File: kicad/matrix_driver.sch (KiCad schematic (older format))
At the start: 54 parts, among them U10 DMN601, U11 NSI45015, U12 SN54LV574, U13 P-FET, U14 NSI45015, U15 DMN601, U16 NSI45015, U17 NSI45015, U18 DMN601, U19 P-FET, U20 NSI45015, U21 74HCT595, U22 NSI45015, U23 DMN601, U24 NSI45015, U25 P-FET, U26 NSI45015, U27 DMN601, U28 NSI45015, U29 SN54LV574, U30 NSI45015, U31 DMN601, U32 NSI45015, U33 P-FET, U34 NSI45015, U35 DMN601, U36 NSI45015, U37 NSI45015, U38 P-FET, U39 DMN601, U40 NSI45015, U41 NSI45015, U42 DMN601, U43 NSI45015, U44 SN54LV574, U45 74HCT595, U46 P-FET, U47 NSI45015, U48 DMN601, U49 NSI45015, U5 NSI45015, U50 NSI45015, U51 DMN601, U52 P-FET, U53 NSI45015, U6 P-FET, U7 DMN601, U8 NSI45015, U9 NSI45015

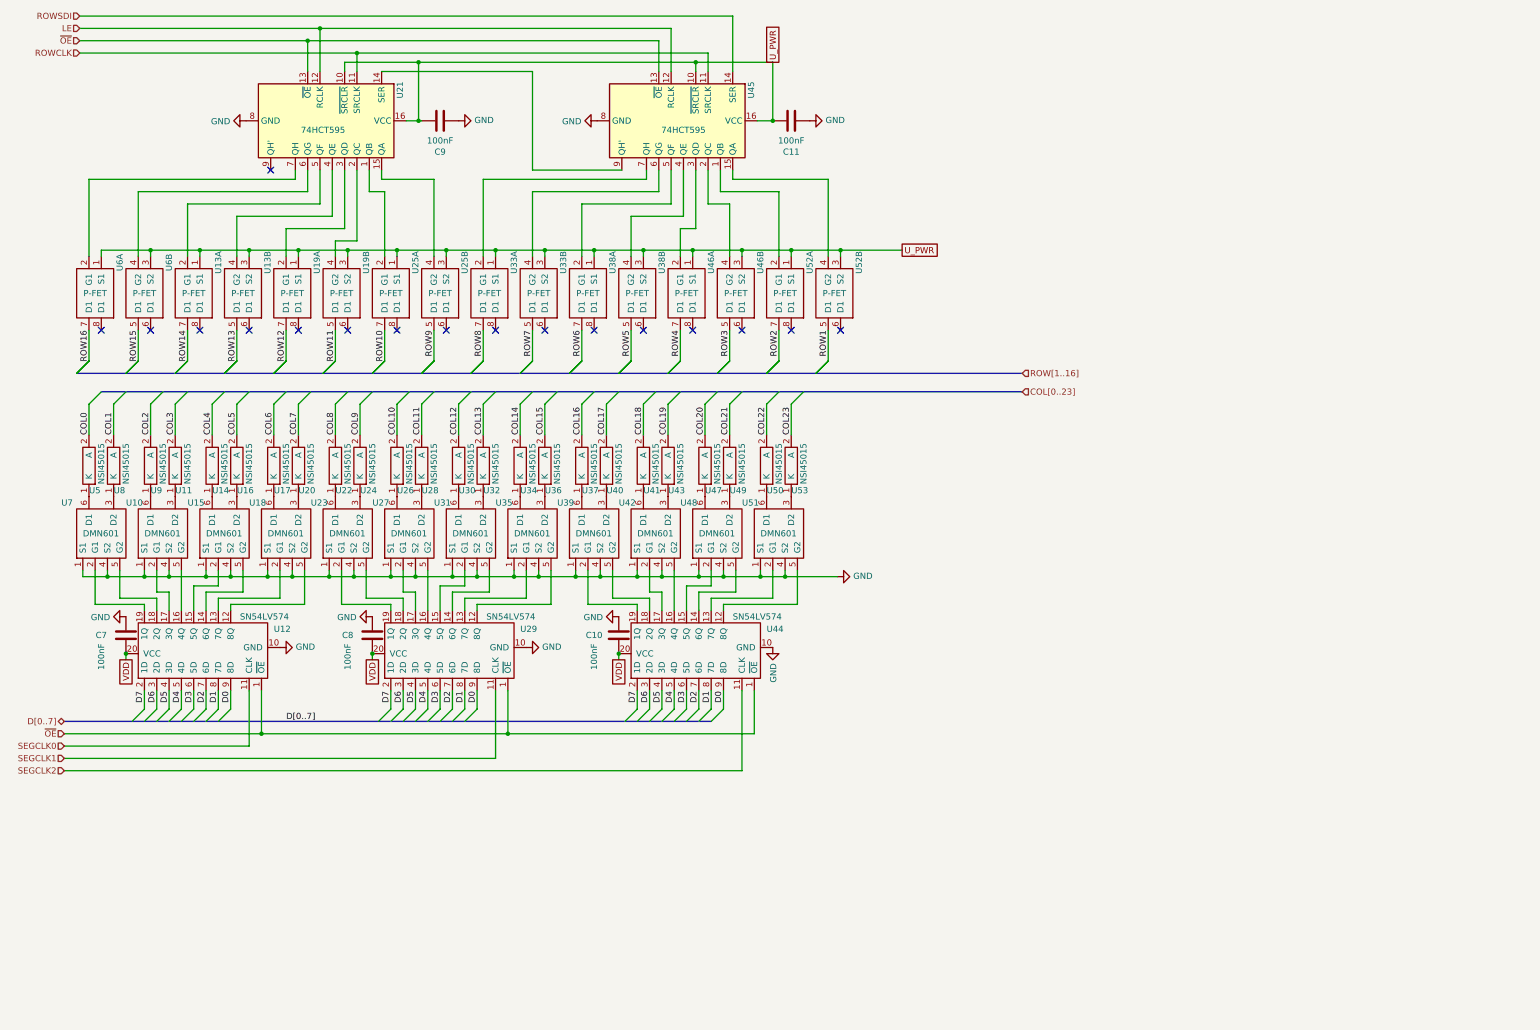
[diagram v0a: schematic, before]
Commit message: Adding level shifters
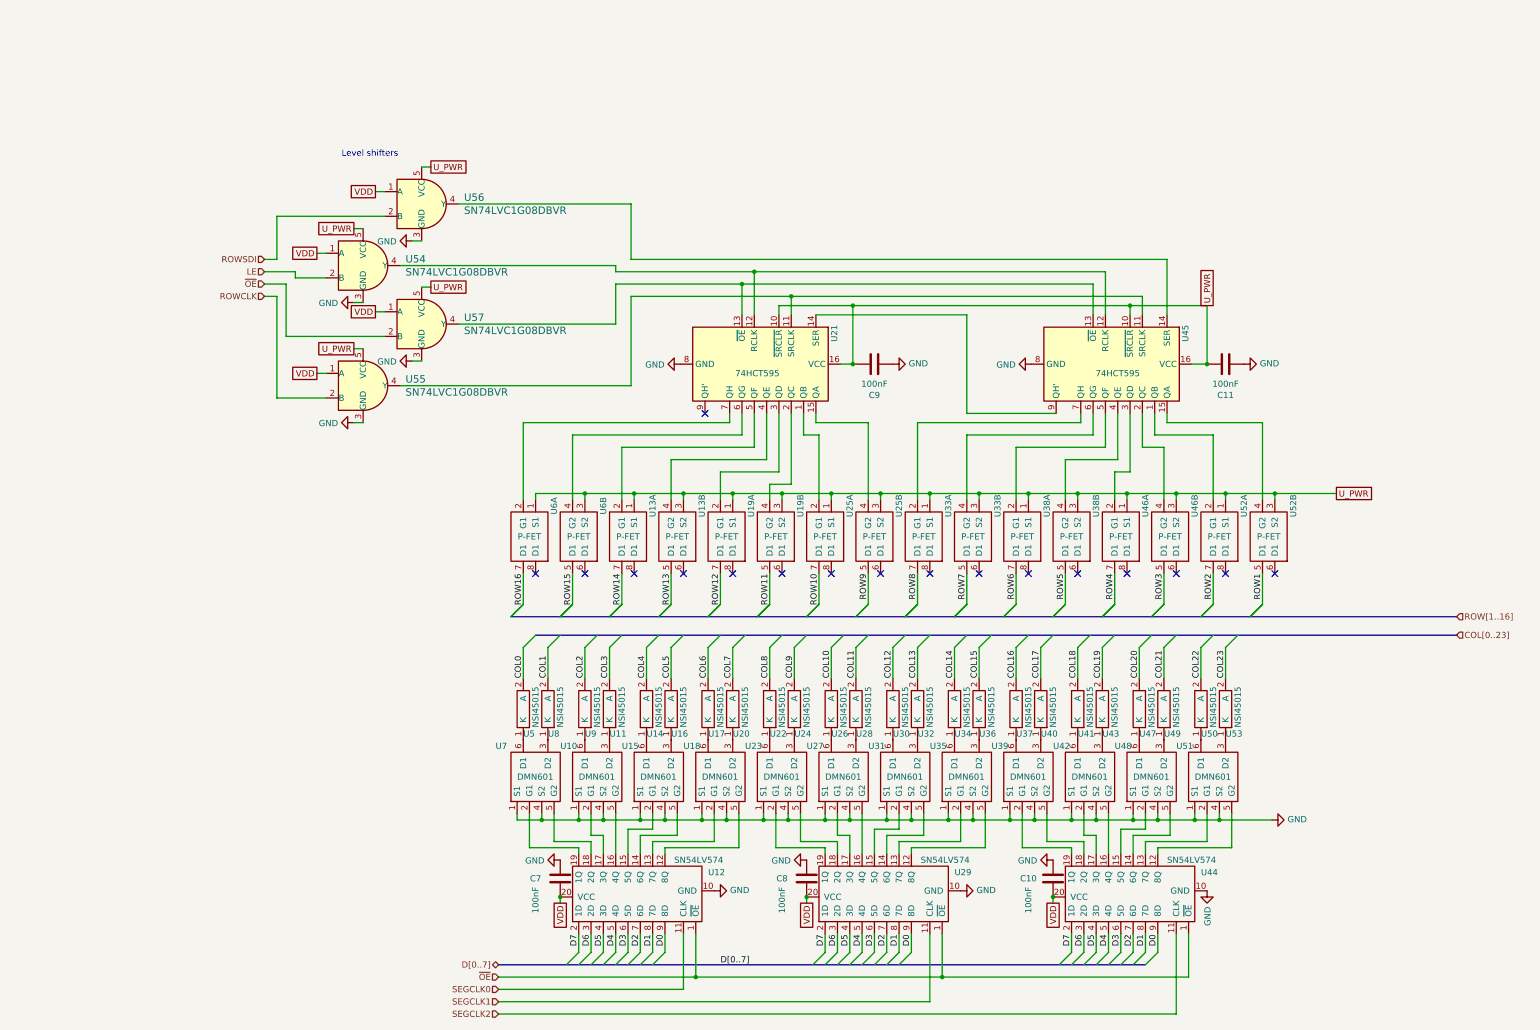
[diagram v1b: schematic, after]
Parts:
- added U54, U55, U56, U57: SN74LVC1G08DBVR, Package_TO_SOT_SMD:SOT-23-5, symbol dk_Logic-Gates-and-Inverters:SN74LVC1G08DBVR
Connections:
- net GND: now also U54.3 (GND), U55.3 (GND), U56.3 (GND), U57.3 (GND)
- net LE: now also U54.2 (B); no longer U21.12 (RCLK), U45.12 (RCLK)
- net ROWCLK: now also U55.2 (B); no longer U21.11 (SRCLK), U45.11 (SRCLK)
- net ROWSDI: now also U56.2 (B); no longer U45.14 (SER)
- net U_PWR: now also U54.5 (VCC), U55.5 (VCC), U56.5 (VCC), U57.5 (VCC)
- net VDD: now also U54.1 (A), U55.1 (A), U56.1 (A), U57.1 (A)
- net ~OE: now also U57.2 (B); no longer U21.13 (~OE), U45.13 (~OE)
- new net: U45.14 (SER), U56.4 (Y)
- new net: U21.13 (~OE), U45.13 (~OE), U57.4 (Y)
- new net: U21.12 (RCLK), U45.12 (RCLK), U54.4 (Y)
- new net: U21.11 (SRCLK), U45.11 (SRCLK), U55.4 (Y)
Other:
- note added: "Level shifters"
- moved on the sheet: C10, C11, C7, C8, C9, U10, U11, U12, U13A, U13B, U14, U15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

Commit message: Fix register footprints and add batt indicator
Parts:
- U12, U29, U44: footprint Package_SO:SO-20_5.3x12.6mm_P1.27mm -> Package_SO:SSOP-20_5.3x7.2mm_P0.65mm
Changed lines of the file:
@@
 F 0 "U44" V 9850 7375 50  0000 R CNN
 F 1 "SN54LV574" V 9950 7650 50  0000 R CNN
-F 2 "Package_SO:SO-20_5.3x12.6mm_P1.27mm" H 9700 7375 50  0001 C CNN
+F 2 "Package_SO:SSOP-20_5.3x7.2mm_P0.65mm" H 9700 7375 50  0001 C CNN
 F 3 "https://www.ti.com/lit/ds/symlink/sn74lv574a.pdf" H 9650 8175 50  0001 C CNN
 	1    9650 8175
@@
 F 0 "U29" V 7850 7375 50  0000 R CNN
 F 1 "SN54LV574" V 7950 7650 50  0000 R CNN
-F 2 "Package_SO:SO-20_5.3x12.6mm_P1.27mm" H 7700 7375 50  0001 C CNN
+F 2 "Package_SO:SSOP-20_5.3x7.2mm_P0.65mm" H 7700 7375 50  0001 C CNN
 F 3 "https://www.ti.com/lit/ds/symlink/sn74lv574a.pdf" H 7650 8175 50  0001 C CNN
 	1    7650 8175
@@
 F 0 "U12" V 5850 7375 50  0000 R CNN
 F 1 "SN54LV574" V 5950 7650 50  0000 R CNN
-F 2 "Package_SO:SO-20_5.3x12.6mm_P1.27mm" H 5700 7375 50  0001 C CNN
+F 2 "Package_SO:SSOP-20_5.3x7.2mm_P0.65mm" H 5700 7375 50  0001 C CNN
 F 3 "https://www.ti.com/lit/ds/symlink/sn74lv574a.pdf" H 5650 8175 50  0001 C CNN
 	1    5650 8175

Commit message: Switched to registers with clear
Also added the mountng holes as annotated symbols with footprints.
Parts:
- U12, U29, U44: value SN54LV574 -> SN74LV573; symbol local:SN54LV574 -> local:SN74LV573
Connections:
- net VDD: now also U12.1 (~OE), U29.1 (~OE), U44.1 (~OE)
- net ~OE: no longer U12.1 (~OE), U29.1 (~OE), U44.1 (~OE)
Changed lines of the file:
@@
 $EndDescr
 $Comp
-L local:SN54LV574 U?
+L local:SN74LV573 U?
 U 1 1 6015CE3D
 P 9650 8175
@@
 AR Path="/6011206E/6015CE3D" Ref="U44"  Part="1"
 F 0 "U44" V 9850 7375 50  0000 R CNN
-F 1 "SN54LV574" V 9950 7650 50  0000 R CNN
+F 1 "SN74LV573" V 9950 7650 50  0000 R CNN
 F 2 "Package_SO:SSOP-20_5.3x7.2mm_P0.65mm" H 9700 7375 50  0001 C CNN
 F 3 "https://www.ti.com/lit/ds/symlink/sn74lv574a.pdf" H 9650 8175 50  0001 C CNN
@@
 Connection ~ 9250 8175
 $Comp
-L local:SN54LV574 U?
+L local:SN74LV573 U?
 U 1 1 6015CF01
 P 7650 8175
@@
 AR Path="/6011206E/6015CF01" Ref="U29"  Part="1"
 F 0 "U29" V 7850 7375 50  0000 R CNN
-F 1 "SN54LV574" V 7950 7650 50  0000 R CNN
+F 1 "SN74LV573" V 7950 7650 50  0000 R CNN
 F 2 "Package_SO:SSOP-20_5.3x7.2mm_P0.65mm" H 7700 7375 50  0001 C CNN
 F 3 "https://www.ti.com/lit/ds/symlink/sn74lv574a.pdf" H 7650 8175 50  0001 C CNN
@@
 	8900 7550 9100 7550
 $Comp
-L local:SN54LV574 U?
+L local:SN74LV573 U?
 U 1 1 6015CF32
 P 5650 8175
@@
 AR Path="/6011206E/6015CF32" Ref="U12"  Part="1"
 F 0 "U12" V 5850 7375 50  0000 R CNN
-F 1 "SN54LV574" V 5950 7650 50  0000 R CNN
+F 1 "SN74LV573" V 5950 7650 50  0000 R CNN
 F 2 "Package_SO:SSOP-20_5.3x7.2mm_P0.65mm" H 5700 7375 50  0001 C CNN
 F 3 "https://www.ti.com/lit/ds/symlink/sn74lv574a.pdf" H 5650 8175 50  0001 C CNN
@@
 Text HLabel 2850 3200 0    50   Input ~ 0
 ~OE
-Wire Wire Line
-	6350 8475 6350 8825
-Wire Wire Line
-	6350 8825 8350 8825
-Wire Wire Line
-	8350 8825 8350 8475
-Wire Wire Line
-	8350 8825 10350 8825
-Wire Wire Line
-	10350 8825 10350 8475
-Connection ~ 8350 8825
-Wire Wire Line
-	4750 8825 6350 8825
-Connection ~ 6350 8825
 Wire Wire Line
 	6250 8475 6250 8925
@@
 Text Notes 3475 2175 0    50   ~ 0
 Level shifters
-Text HLabel 4750 8825 0    50   Input ~ 0
-~OE
 Wire Bus Line
 	4850 5900 12525 5900
@@
 Wire Bus Line
 	4750 8725 10000 8725
+Text GLabel 6350 8475 3    50   UnSpc ~ 0
+VDD
+Text GLabel 8350 8475 3    50   UnSpc ~ 0
+VDD
+Text GLabel 10350 8475 3    50   UnSpc ~ 0
+VDD
 $EndSCHEMATC

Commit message: Reduce pad with for SSOP-20 footprint
This ensures there's solder mask between the pads.
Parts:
- U12, U29, U44: footprint Package_SO:SSOP-20_5.3x7.2mm_P0.65mm -> local:SSOP-20_W5.3mm
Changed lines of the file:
@@
 F 0 "U44" V 9850 7375 50  0000 R CNN
 F 1 "SN74LV573" V 9950 7650 50  0000 R CNN
-F 2 "Package_SO:SSOP-20_5.3x7.2mm_P0.65mm" H 9700 7375 50  0001 C CNN
+F 2 "local:SSOP-20_W5.3mm" H 9700 7375 50  0001 C CNN
 F 3 "https://www.ti.com/lit/ds/symlink/sn74lv574a.pdf" H 9650 8175 50  0001 C CNN
 	1    9650 8175
@@
 F 0 "U29" V 7850 7375 50  0000 R CNN
 F 1 "SN74LV573" V 7950 7650 50  0000 R CNN
-F 2 "Package_SO:SSOP-20_5.3x7.2mm_P0.65mm" H 7700 7375 50  0001 C CNN
+F 2 "local:SSOP-20_W5.3mm" H 7700 7375 50  0001 C CNN
 F 3 "https://www.ti.com/lit/ds/symlink/sn74lv574a.pdf" H 7650 8175 50  0001 C CNN
 	1    7650 8175
@@
 F 0 "U12" V 5850 7375 50  0000 R CNN
 F 1 "SN74LV573" V 5950 7650 50  0000 R CNN
-F 2 "Package_SO:SSOP-20_5.3x7.2mm_P0.65mm" H 5700 7375 50  0001 C CNN
+F 2 "local:SSOP-20_W5.3mm" H 5700 7375 50  0001 C CNN
 F 3 "https://www.ti.com/lit/ds/symlink/sn74lv574a.pdf" H 5650 8175 50  0001 C CNN
 	1    5650 8175
@@
 Text Notes 3475 2175 0    50   ~ 0
 Level shifters
+Text GLabel 6350 8475 3    50   UnSpc ~ 0
+VDD
+Text GLabel 8350 8475 3    50   UnSpc ~ 0
+VDD
+Text GLabel 10350 8475 3    50   UnSpc ~ 0
+VDD
 Wire Bus Line
 	4850 5900 12525 5900
@@
 Wire Bus Line
 	4750 8725 10000 8725
-Text GLabel 6350 8475 3    50   UnSpc ~ 0
-VDD
-Text GLabel 8350 8475 3    50   UnSpc ~ 0
-VDD
-Text GLabel 10350 8475 3    50   UnSpc ~ 0
-VDD
 $EndSCHEMATC

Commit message: Swith back to 74LV573 flip-flop
This changes switches back to the original 74LV573 octal flip-flop
instead of the 273. This due to the pinout difference and the fact
that the board already followed the pinout of th 573.

Package is still SSOP-20.
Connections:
- net GND: now also U12.1 (~OE), U29.1 (~OE), U44.1 (~OE)
- net VDD: no longer U12.1 (~OE), U29.1 (~OE), U44.1 (~OE)
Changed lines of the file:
@@
 F 3 "" H 10500 8125 50  0001 C CNN
 	1    10500 8125
-	1    0    0    -1
+	0    -1   -1   0
 $EndComp
 Wire Wire Line
@@
 Text Notes 3475 2175 0    50   ~ 0
 Level shifters
-Text GLabel 6350 8475 3    50   UnSpc ~ 0
-VDD
-Text GLabel 8350 8475 3    50   UnSpc ~ 0
-VDD
-Text GLabel 10350 8475 3    50   UnSpc ~ 0
-VDD
+Wire Wire Line
+	10500 8125 10500 8475
+Wire Wire Line
+	10500 8475 10350 8475
+Connection ~ 10500 8125
+Wire Wire Line
+	6500 8125 6500 8475
+Wire Wire Line
+	6350 8475 6500 8475
+Connection ~ 6500 8125
+Wire Wire Line
+	8500 8125 8500 8475
+Wire Wire Line
+	8350 8475 8500 8475
 Wire Bus Line
 	4850 5900 12525 5900
@@
 Wire Bus Line
 	4750 8725 10000 8725
+Connection ~ 8500 8125
 $EndSCHEMATC

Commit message: Switched back to SOIC-20 package for the 74LV573s
Because they're easier to solder and we've got enough space.
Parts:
- U12, U29, U44: footprint local:SSOP-20_W5.3mm -> Package_SO:SO-20_5.3x12.6mm_P1.27mm
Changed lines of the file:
@@
 F 0 "U44" V 9850 7375 50  0000 R CNN
 F 1 "SN74LV573" V 9950 7650 50  0000 R CNN
-F 2 "local:SSOP-20_W5.3mm" H 9700 7375 50  0001 C CNN
+F 2 "Package_SO:SO-20_5.3x12.6mm_P1.27mm" H 9700 7375 50  0001 C CNN
 F 3 "https://www.ti.com/lit/ds/symlink/sn74lv574a.pdf" H 9650 8175 50  0001 C CNN
 	1    9650 8175
@@
 F 0 "U29" V 7850 7375 50  0000 R CNN
 F 1 "SN74LV573" V 7950 7650 50  0000 R CNN
-F 2 "local:SSOP-20_W5.3mm" H 7700 7375 50  0001 C CNN
+F 2 "Package_SO:SO-20_5.3x12.6mm_P1.27mm" H 7700 7375 50  0001 C CNN
 F 3 "https://www.ti.com/lit/ds/symlink/sn74lv574a.pdf" H 7650 8175 50  0001 C CNN
 	1    7650 8175
@@
 F 0 "U12" V 5850 7375 50  0000 R CNN
 F 1 "SN74LV573" V 5950 7650 50  0000 R CNN
-F 2 "local:SSOP-20_W5.3mm" H 5700 7375 50  0001 C CNN
+F 2 "Package_SO:SO-20_5.3x12.6mm_P1.27mm" H 5700 7375 50  0001 C CNN
 F 3 "https://www.ti.com/lit/ds/symlink/sn74lv574a.pdf" H 5650 8175 50  0001 C CNN
 	1    5650 8175
@@
 Wire Wire Line
 	8350 8475 8500 8475
+Connection ~ 8500 8125
 Wire Bus Line
 	4850 5900 12525 5900
@@
 Wire Bus Line
 	4750 8725 10000 8725
-Connection ~ 8500 8125
 $EndSCHEMATC
